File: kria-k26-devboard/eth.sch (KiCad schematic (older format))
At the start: 41 parts, among them J5 5-2337992-8, Q4 BSS138DW-7-F, U21 DP83867CRRGZR, Y7 ECS-2016MV-250-CN-TR3

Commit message: Misc. signals routing, routed REF_CLK's, PS Power plane creation
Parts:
- removed Q4: BSS138DW-7-F, antmicro-footprints:SOT-363, symbol antmicroTransistorsFETsMOSFETsArrays:BSS138DW-7-F
- added C185: C_100n_0402, antmicro-footprints:0402-cap, symbol antmicroCapacitors0402:C_100n_0402
- added Q16, Q4: DTC014TEBTL, antmicro-footprints:SOT-416, symbol antmicroTransistorsBipolarSingle:DTC014TEBTL
- added R148: R_330R_0402, antmicro-footprints:0402-res, symbol antmicroResistors0402:R_330R_0402
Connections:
- wire segments 222 -> 229
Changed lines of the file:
@@
 Wire Wire Line
 	8050 4400 10200 4400
-$Comp
-L power:GND #PWR0101
-U 1 1 6234FEAD
-P 10150 5400
-F 0 "#PWR0101" H 10150 5150 50  0001 C CNN
-F 1 "GND" H 10155 5227 50  0000 C CNN
-F 2 "" H 10150 5400 50  0001 C CNN
-F 3 "" H 10150 5400 50  0001 C CNN
-	1    10150 5400
-	1    0    0    -1
-$EndComp
 Wire Wire Line
 	10150 5150 10150 5250
 Wire Wire Line
 	10200 5250 10150 5250
-Connection ~ 10150 5250
-Wire Wire Line
-	10150 5250 10150 5400
 Wire Wire Line
 	10150 5150 10200 5150
@@
 MIO76
 $Comp
-L antmicroTransistorsFETsMOSFETsArrays:BSS138DW-7-F Q4
-U 1 1 6251B827
-P 12100 4800
-F 0 "Q4" H 12050 5287 60  0000 C CNN
-F 1 "BSS138DW-7-F" H 12050 5181 60  0000 C CNN
-F 2 "antmicro-footprints:SOT-363" H 12300 5000 60  0001 L CNN
-F 3 "https://www.diodes.com/assets/Datasheets/ds30203.pdf" V 12300 5100 60  0001 L CNN
-F 4 "BSS138DW-7-F" H 12300 5300 60  0001 L CNN "MPN"
-F 5 "Diodes Incorporated" H 12300 5900 60  0001 L CNN "Manufacturer"
-	1    12100 4800
-	0    -1   -1   0
-$EndComp
-$Comp
 L power:GND #PWR0102
 U 1 1 62553413
-P 11900 5150
-F 0 "#PWR0102" H 11900 4900 50  0001 C CNN
-F 1 "GND" H 11905 4977 50  0000 C CNN
-F 2 "" H 11900 5150 50  0001 C CNN
-F 3 "" H 11900 5150 50  0001 C CNN
-	1    11900 5150
-	1    0    0    -1
-$EndComp
-Wire Wire Line
-	11900 5150 11900 5100
-$Comp
-L power:GND #PWR0103
-U 1 1 6255A8E4
-P 12700 4650
-F 0 "#PWR0103" H 12700 4400 50  0001 C CNN
-F 1 "GND" H 12705 4477 50  0000 C CNN
-F 2 "" H 12700 4650 50  0001 C CNN
-F 3 "" H 12700 4650 50  0001 C CNN
-	1    12700 4650
-	1    0    0    -1
-$EndComp
-Wire Wire Line
-	12500 4600 12500 4550
-Wire Wire Line
-	12500 4550 12700 4550
-Wire Wire Line
-	12700 4550 12700 4650
+P 11900 5050
+F 0 "#PWR0102" H 11900 4800 50  0001 C CNN
+F 1 "GND" H 11905 4877 50  0000 C CNN
+F 2 "" H 11900 5050 50  0001 C CNN
+F 3 "" H 11900 5050 50  0001 C CNN
+	1    11900 5050
+	1    0    0    -1
+$EndComp
+Wire Wire Line
+	11900 5050 11900 5000
 Wire Wire Line
 	7550 4900 7700 4900
@@
 Text Label 7650 5500 0    50   ~ 0
 LED1
-Text Label 12200 4500 1    50   ~ 0
+Text Label 12950 4850 0    50   ~ 0
 LED1
-Text Label 12200 5200 3    50   ~ 0
+Text Label 11450 4800 2    50   ~ 0
 LED2
 Wire Wire Line
-	12200 5200 12200 5100
-Wire Wire Line
-	12200 4600 12200 4500
+	11450 4800 11550 4800
+Wire Wire Line
+	12850 4850 12950 4850
 Wire Wire Line
 	11900 4600 11900 4350
 Wire Wire Line
 	11300 4350 11900 4350
-Wire Wire Line
-	12850 4050 12850 5200
-Wire Wire Line
-	12850 5200 12500 5200
-Wire Wire Line
-	12500 5200 12500 5100
 $Comp
 L antmicroResistors0402:R_330R_0402 R56
@@
 	11300 4250 11900 4250
 Wire Wire Line
-	11300 4050 12850 4050
+	11300 4050 12400 4050
 Wire Wire Line
 	12500 4150 12500 3750
@@
 Text Label 4600 8700 0    50   ~ 0
 X_I
+$Comp
+L antmicroTransistorsBipolarSingle:DTC014TEBTL Q4
+U 1 1 62F64364
+P 11800 4800
+F 0 "Q4" H 11750 5000 50  0000 L CNN
+F 1 "DTC014TEBTL" H 11350 4600 50  0000 L CNN
+F 2 "antmicro-footprints:SOT-416" H 12000 4500 50  0001 L CNN
+F 3 "" H 11800 4800 50  0001 L CNN
+F 4 "ROHM Semiconductor" H 12400 4700 50  0001 C CNN "Manufacturer"
+F 5 "DTC014TEBTL" H 12250 4600 50  0001 C CNN "MPN"
+	1    11800 4800
+	1    0    0    -1
+$EndComp
+$Comp
+L antmicroTransistorsBipolarSingle:DTC014TEBTL Q16
+U 1 1 62FA085F
+P 12600 4850
+F 0 "Q16" H 12500 5050 50  0000 L CNN
+F 1 "DTC014TEBTL" H 12100 4650 50  0000 L CNN
+F 2 "antmicro-footprints:SOT-416" H 12800 4550 50  0001 L CNN
+F 3 "" H 12600 4850 50  0001 L CNN
+F 4 "ROHM Semiconductor" H 13200 4750 50  0001 C CNN "Manufacturer"
+F 5 "DTC014TEBTL" H 13050 4650 50  0001 C CNN "MPN"
+	1    12600 4850
+	-1   0    0    -1
+$EndComp
+Wire Wire Line
+	12400 4050 12400 4500
+Wire Wire Line
+	12400 4500 12500 4500
+Wire Wire Line
+	12500 4500 12500 4650
+$Comp
+L power:GND #PWR0103
+U 1 1 62FE7102
+P 12500 5100
+F 0 "#PWR0103" H 12500 4850 50  0001 C CNN
+F 1 "GND" H 12505 4927 50  0000 C CNN
+F 2 "" H 12500 5100 50  0001 C CNN
+F 3 "" H 12500 5100 50  0001 C CNN
+	1    12500 5100
+	1    0    0    -1
+$EndComp
+Wire Wire Line
+	12500 5100 12500 5050
+$Comp
+L antmicroResistors0402:R_330R_0402 R?
+U 1 1 630DAD7C
+P 9950 5600
+AR Path="/63CADD16/630DAD7C" Ref="R?"  Part="1"
+AR Path="/63C3FA95/630DAD7C" Ref="R148"  Part="1"
+F 0 "R148" V 9905 5670 60  0000 L CNN
+F 1 "R_330R_0402" H 9950 5450 60  0001 C CNN
+F 2 "antmicro-footprints:0402-res" H 10150 5800 60  0001 L CNN
+F 3 "" H 9950 5600 50  0001 C CNN
+F 4 "MULTICOMP" H 10150 6000 60  0001 L CNN "Manufacturer"
+F 5 "MCMR04X3300FTL" H 10150 5900 60  0001 L CNN "MPN"
+F 6 "330R" H 9850 5600 50  0000 L CNN "Val"
+	1    9950 5600
+	0    1    1    0
+$EndComp
+$Comp
+L antmicroCapacitors0402:C_100n_0402 C?
+U 1 1 630DAD85
+P 10250 5600
+AR Path="/63CADD16/630DAD85" Ref="C?"  Part="1"
+AR Path="/63C3FA95/630DAD85" Ref="C185"  Part="1"
+F 0 "C185" H 10365 5645 60  0000 L CNN
+F 1 "C_100n_0402" H 10250 5450 60  0001 C CNN
+F 2 "antmicro-footprints:0402-cap" H 10450 5800 60  0001 L CNN
+F 3 "" H 10250 5600 50  0001 C CNN
+F 4 "Murata" H 10450 6000 60  0001 L CNN "Manufacturer"
+F 5 "GRM155R61H104KE14D" H 10450 5900 60  0001 L CNN "MPN"
+F 6 "100n" H 10365 5547 50  0000 L CNN "Val"
+	1    10250 5600
+	1    0    0    -1
+$EndComp
+Wire Wire Line
+	9950 5750 9950 5800
+Wire Wire Line
+	9950 5800 10100 5800
+Wire Wire Line
+	10100 5850 10100 5800
+Connection ~ 10100 5800
+Wire Wire Line
+	10100 5800 10250 5800
+Wire Wire Line
+	10250 5800 10250 5750
+$Comp
+L power:GND #PWR?
+U 1 1 630DAD91
+P 10100 5850
+AR Path="/63CADD16/630DAD91" Ref="#PWR?"  Part="1"
+AR Path="/63C3FA95/630DAD91" Ref="#PWR0101"  Part="1"
+F 0 "#PWR0101" H 10100 5600 50  0001 C CNN
+F 1 "GND" H 10105 5677 50  0000 C CNN
+F 2 "" H 10100 5850 50  0001 C CNN
+F 3 "" H 10100 5850 50  0001 C CNN
+	1    10100 5850
+	1    0    0    -1
+$EndComp
+Wire Wire Line
+	10250 5450 10250 5400
+Wire Wire Line
+	10250 5400 10150 5400
+Wire Wire Line
+	9950 5400 9950 5450
+Wire Wire Line
+	10150 5250 10150 5400
 Wire Bus Line
 	8500 5900 8500 6100
@@
 Wire Bus Line
 	4600 3250 4600 4800
+Connection ~ 10150 5250
+Connection ~ 10150 5400
+Wire Wire Line
+	10150 5400 9950 5400
 $EndSCHEMATC

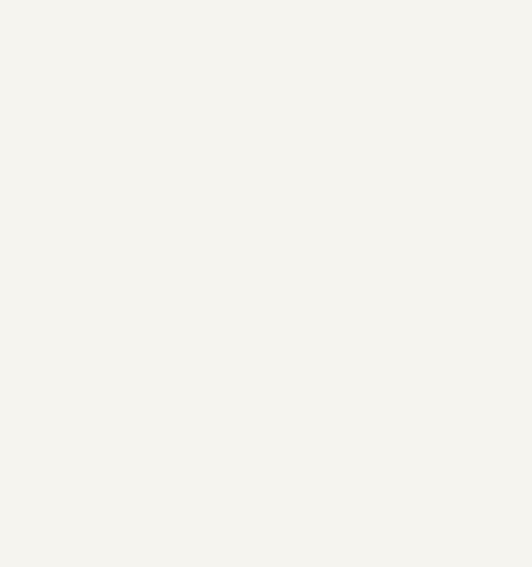
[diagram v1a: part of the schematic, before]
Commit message: Fixed possible FTDI-USB backfeeding issue, finished PS and FTDI power planes creation, finished routing of FTDI/Debug part
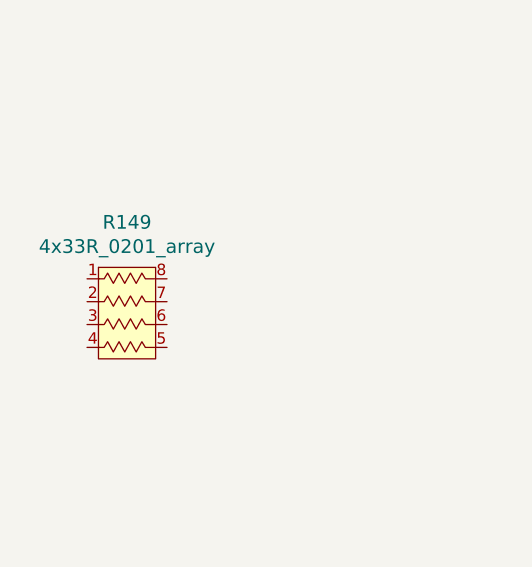
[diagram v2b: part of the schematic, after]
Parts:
- added R149: 4x33R_0201_array, antmicro-footprints:EXB18V, symbol antmicroResistorNetworksArrays:4x33R_0201_array
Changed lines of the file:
@@
 Wire Wire Line
 	10150 5400 9950 5400
+$Comp
+L antmicroResistorNetworksArrays:4x33R_0201_array R149
+U 1 1 632CC1BA
+P -3650 3550
+F 0 "R149" H -3675 4197 60  0000 C CNN
+F 1 "4x33R_0201_array" H -3675 4091 60  0000 C CNN
+F 2 "antmicro-footprints:EXB18V" H -3850 4300 60  0001 L CNN
+F 3 "http://industrial.panasonic.com/cdbs/www-data/pdf/AOC0000/AOC0000C14.pdf" H -3850 4300 60  0001 L CNN
+F 4 "EXB-18V330JX" H -3850 4500 60  0001 L CNN "MPN"
+F 5 "Panasonic" H -3850 4400 60  0001 L CNN "Manufacturer"
+	1    -3650 3550
+	1    0    0    -1
+$EndComp
 $EndSCHEMATC

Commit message: Optimization of power planes, fixed missing capacitors on USB 3.0, unify shields, polishing of layout
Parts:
- removed C185: C_100n_0402, antmicro-footprints:0402-cap, symbol antmicroCapacitors0402:C_100n_0402
- removed R148: R_330R_0402, antmicro-footprints:0402-res, symbol antmicroResistors0402:R_330R_0402
- removed R149: 4x33R_0201_array, antmicro-footprints:EXB18V, symbol antmicroResistorNetworksArrays:4x33R_0201_array
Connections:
- net SH_UP: now reaches J5.19 (SHIELD1), J5.20 (SHIELD2)
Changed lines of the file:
@@
 Wire Wire Line
 	12500 5100 12500 5050
-$Comp
-L antmicroResistors0402:R_330R_0402 R?
-U 1 1 630DAD7C
-P 9950 5600
-AR Path="/63CADD16/630DAD7C" Ref="R?"  Part="1"
-AR Path="/63C3FA95/630DAD7C" Ref="R148"  Part="1"
-F 0 "R148" V 9905 5670 60  0000 L CNN
-F 1 "R_330R_0402" H 9950 5450 60  0001 C CNN
-F 2 "antmicro-footprints:0402-res" H 10150 5800 60  0001 L CNN
-F 3 "" H 9950 5600 50  0001 C CNN
-F 4 "MULTICOMP" H 10150 6000 60  0001 L CNN "Manufacturer"
-F 5 "MCMR04X3300FTL" H 10150 5900 60  0001 L CNN "MPN"
-F 6 "330R" H 9850 5600 50  0000 L CNN "Val"
-	1    9950 5600
-	0    1    1    0
-$EndComp
-$Comp
-L antmicroCapacitors0402:C_100n_0402 C?
-U 1 1 630DAD85
-P 10250 5600
-AR Path="/63CADD16/630DAD85" Ref="C?"  Part="1"
-AR Path="/63C3FA95/630DAD85" Ref="C185"  Part="1"
-F 0 "C185" H 10365 5645 60  0000 L CNN
-F 1 "C_100n_0402" H 10250 5450 60  0001 C CNN
-F 2 "antmicro-footprints:0402-cap" H 10450 5800 60  0001 L CNN
-F 3 "" H 10250 5600 50  0001 C CNN
-F 4 "Murata" H 10450 6000 60  0001 L CNN "Manufacturer"
-F 5 "GRM155R61H104KE14D" H 10450 5900 60  0001 L CNN "MPN"
-F 6 "100n" H 10365 5547 50  0000 L CNN "Val"
-	1    10250 5600
-	1    0    0    -1
-$EndComp
-Wire Wire Line
-	9950 5750 9950 5800
-Wire Wire Line
-	9950 5800 10100 5800
-Wire Wire Line
-	10100 5850 10100 5800
-Connection ~ 10100 5800
-Wire Wire Line
-	10100 5800 10250 5800
-Wire Wire Line
-	10250 5800 10250 5750
-$Comp
-L power:GND #PWR?
-U 1 1 630DAD91
-P 10100 5850
-AR Path="/63CADD16/630DAD91" Ref="#PWR?"  Part="1"
-AR Path="/63C3FA95/630DAD91" Ref="#PWR0101"  Part="1"
-F 0 "#PWR0101" H 10100 5600 50  0001 C CNN
-F 1 "GND" H 10105 5677 50  0000 C CNN
-F 2 "" H 10100 5850 50  0001 C CNN
-F 3 "" H 10100 5850 50  0001 C CNN
-	1    10100 5850
-	1    0    0    -1
-$EndComp
-Wire Wire Line
-	10250 5450 10250 5400
-Wire Wire Line
-	10250 5400 10150 5400
-Wire Wire Line
-	9950 5400 9950 5450
 Wire Wire Line
 	10150 5250 10150 5400
 Connection ~ 10150 5250
-Connection ~ 10150 5400
-Wire Wire Line
-	10150 5400 9950 5400
-$Comp
-L antmicroResistorNetworksArrays:4x33R_0201_array R149
-U 1 1 632CC1BA
-P -3650 3550
-F 0 "R149" H -3675 4197 60  0000 C CNN
-F 1 "4x33R_0201_array" H -3675 4091 60  0000 C CNN
-F 2 "antmicro-footprints:EXB18V" H -3850 4300 60  0001 L CNN
-F 3 "http://industrial.panasonic.com/cdbs/www-data/pdf/AOC0000/AOC0000C14.pdf" H -3850 4300 60  0001 L CNN
-F 4 "EXB-18V330JX" H -3850 4500 60  0001 L CNN "MPN"
-F 5 "Panasonic" H -3850 4400 60  0001 L CNN "Manufacturer"
-	1    -3650 3550
-	1    0    0    -1
-$EndComp
 Wire Bus Line
 	8500 5900 8500 6100
@@
 Wire Bus Line
 	4600 3250 4600 4800
+Text GLabel 10150 5400 3    50   Input ~ 0
+SH_UP
 $EndSCHEMATC

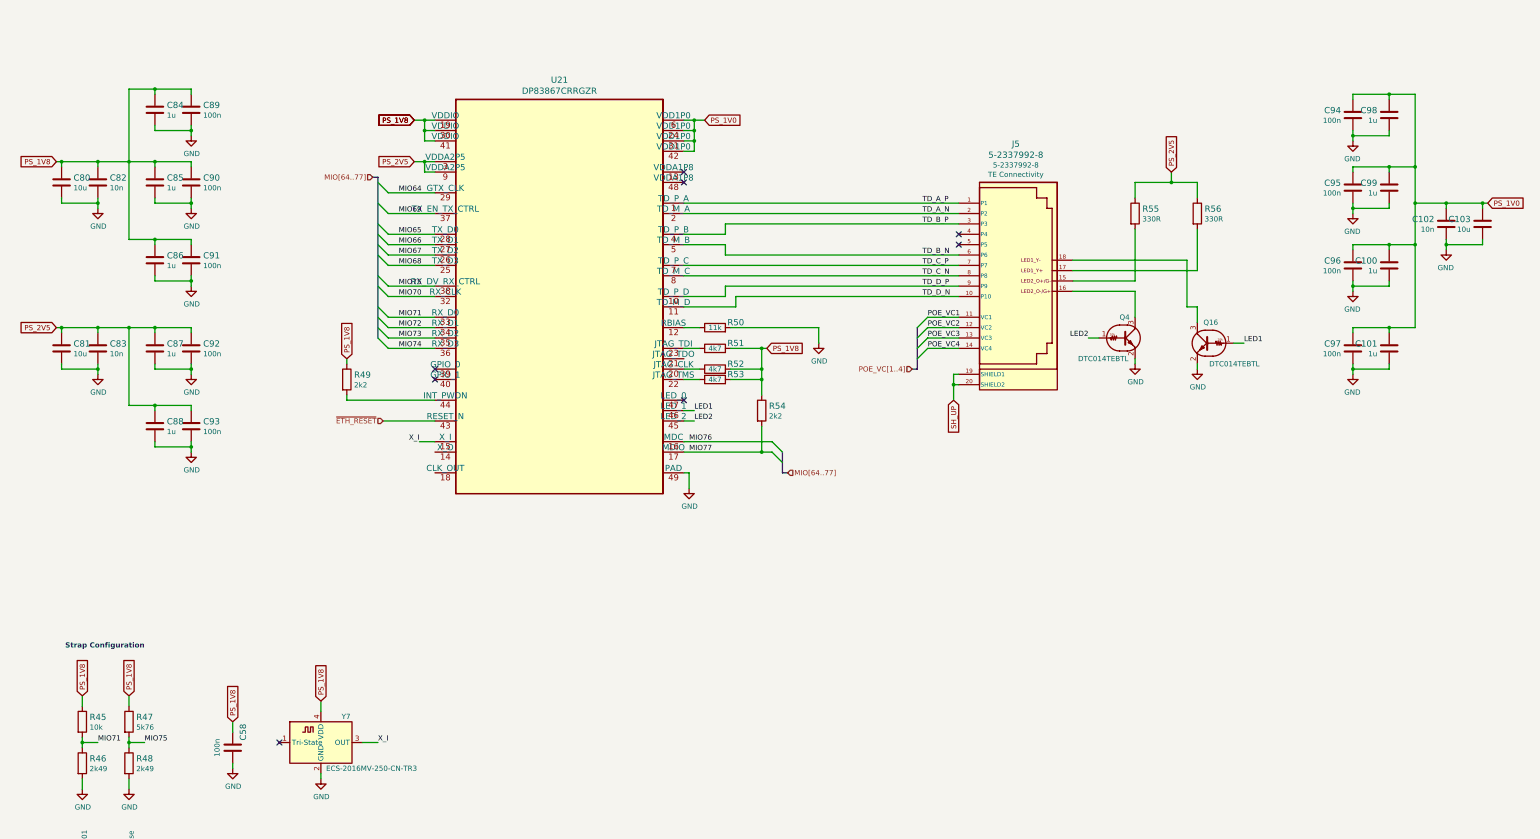
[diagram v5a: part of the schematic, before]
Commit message: Fixed missing USB - M2 connection, finishing touches of PCB
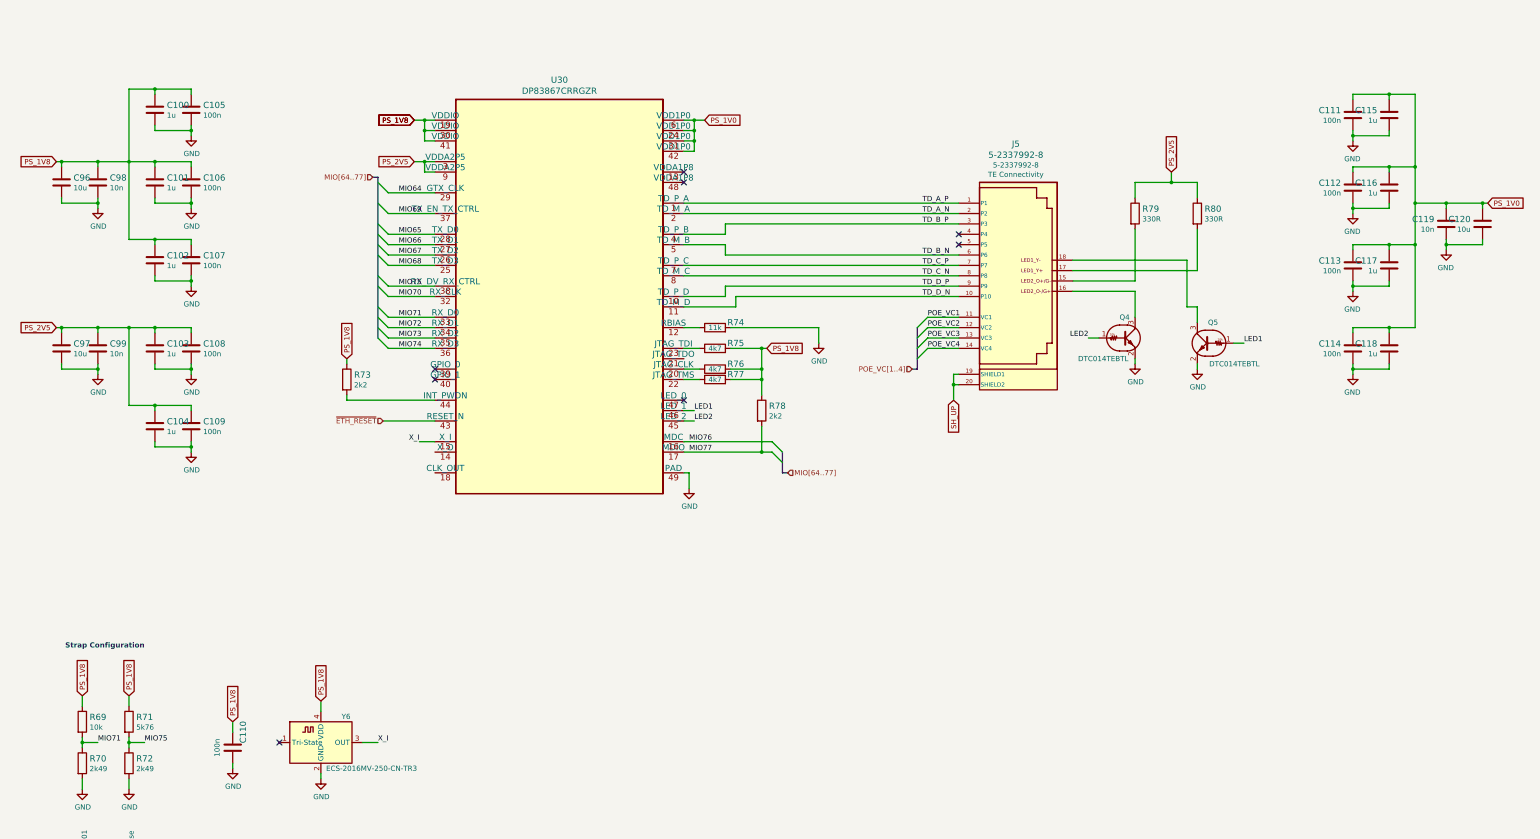
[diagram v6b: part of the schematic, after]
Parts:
- renumbered C84 to C100, C85 to C101, C86 to C102, C87 to C103, C88 to C104, C89 to C105, C90 to C106, C91 to C107, C92 to C108, C93 to C109, C58 to C110, C94 to C111, C95 to C112, C96 to C113, C97 to C114, C98 to C115, C99 to C116, C100 to C117, C101 to C118, C102 to C119, C103 to C120, C80 to C96, C81 to C97, C82 to C98, C83 to C99, Q16 to Q5, R45 to R69, R46 to R70, R47 to R71, R48 to R72, R49 to R73, R50 to R74, R51 to R75, R52 to R76, R53 to R77, R54 to R78, R55 to R79, R56 to R80, U21 to U30, Y7 to Y6

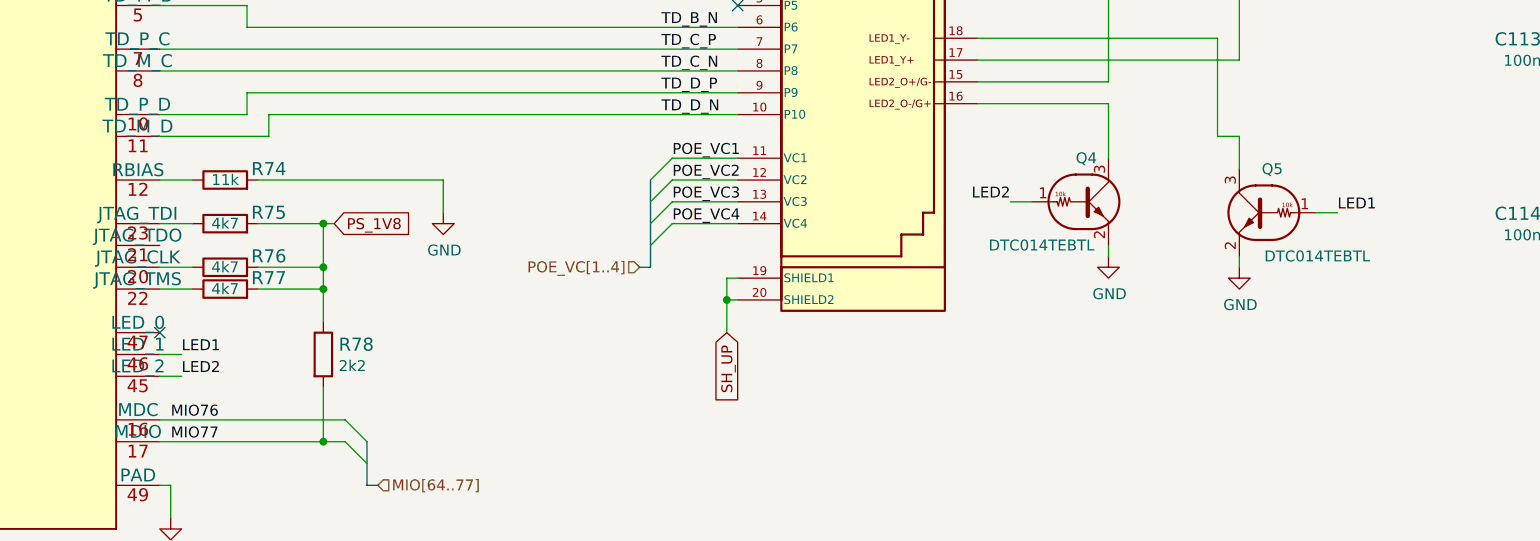
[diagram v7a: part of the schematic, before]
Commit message: Finished implementing changes after the review, fixed ETH led connections, length matching fixed and double checked with external script
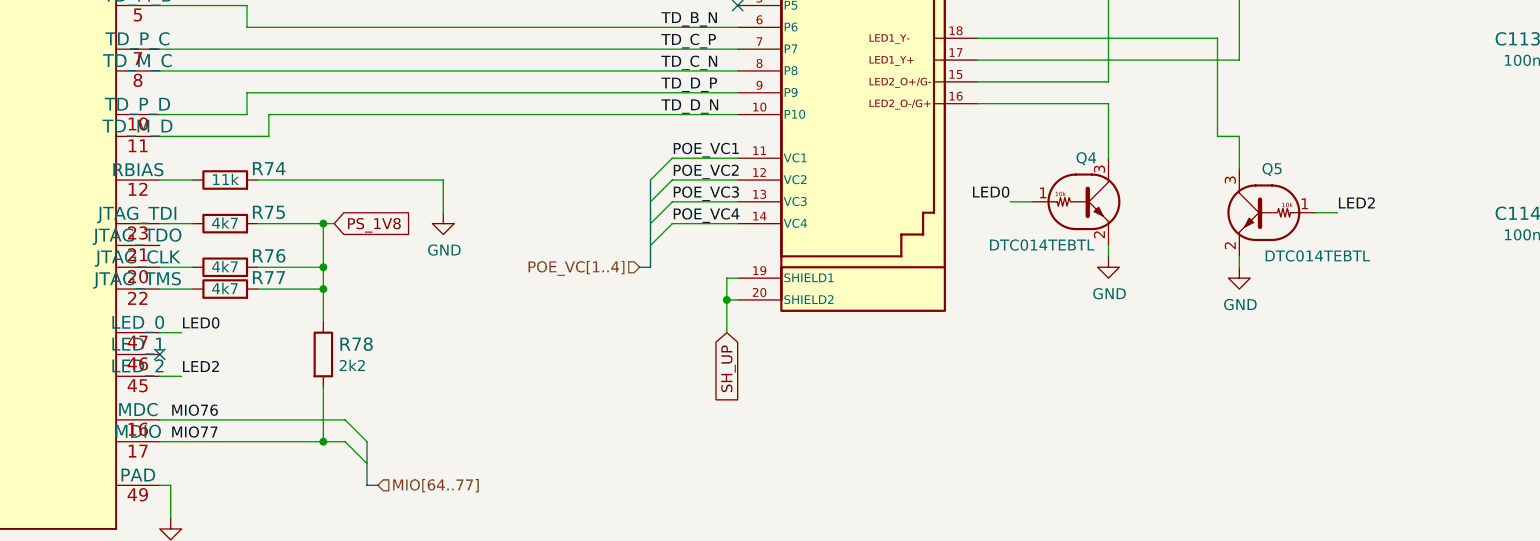
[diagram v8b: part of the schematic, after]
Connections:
- net LED2: now also Q5.1 (B); no longer Q4.1 (B)
- net LED0: now reaches U30.47 (LED_0)
- net LED0: now also Q4.1 (B)
- net LED1: no longer names the net of U30.46 (LED_1)
- net LED1: no longer Q5.1 (B)
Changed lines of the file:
@@
 encoding utf-8
 Sheet 9 19
-Title ""
+Title "ETH PHY"
 Date "2022-03-10"
 Rev "1.0.0"
@@
 Wire Wire Line
 	8850 4700 8850 4850
-Wire Wire Line
-	7550 5500 7650 5500
-Text Label 7650 5500 0    50   ~ 0
-LED1
-Text Label 12950 4850 0    50   ~ 0
-LED1
-Text Label 11450 4800 2    50   ~ 0
-LED2
+Text Label 7650 5400 0    50   ~ 0
+LED0
 Wire Wire Line
 	11450 4800 11550 4800
@@
 	1    0    0    -1
 $EndComp
-NoConn ~ 7550 5400
 NoConn ~ 7550 3200
 NoConn ~ 7550 3300
@@
 Text GLabel 10150 5400 3    50   Input ~ 0
 SH_UP
+Wire Wire Line
+	7550 5400 7650 5400
+NoConn ~ 7550 5500
+Text Label 12950 4850 0    50   ~ 0
+LED2
 Wire Bus Line
 	8500 5900 8500 6100
@@
 Wire Bus Line
 	4600 3250 4600 4800
+Text Label 11450 4800 2    50   ~ 0
+LED0
 $EndSCHEMATC
